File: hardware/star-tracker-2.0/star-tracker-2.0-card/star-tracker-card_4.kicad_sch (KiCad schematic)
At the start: 18 parts, among them U10 RCLAMP0504FB, U7 OSD3358-512M-BSM, Y1 ECS-240-12-30BQ-AEN-TR, Y2 ABS07-32.768KHZ-T

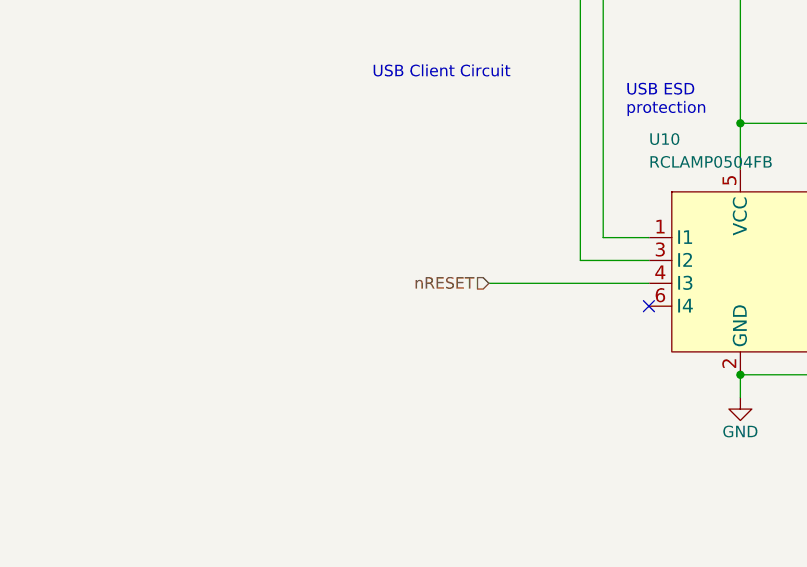
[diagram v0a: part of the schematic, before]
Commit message: Updated USB clamp
minor routing and schematic changes. Updated OPD with new transistors. Changed resistor values on LEDs.
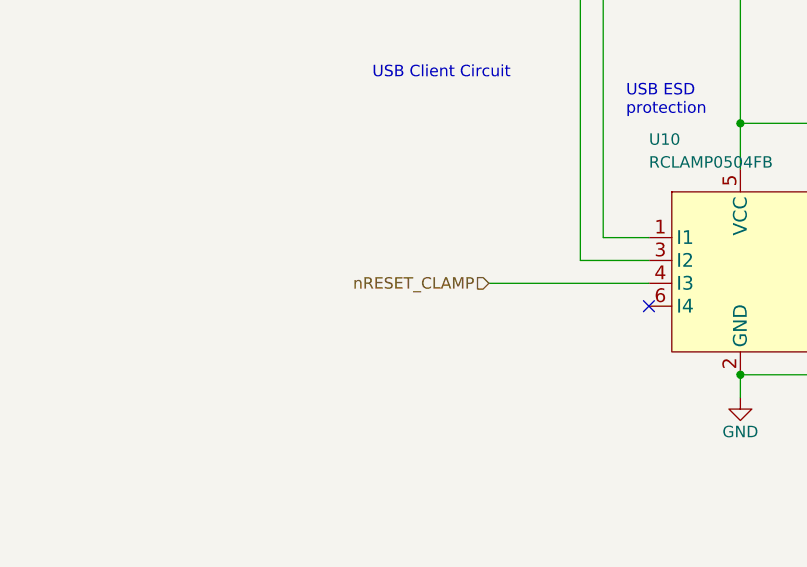
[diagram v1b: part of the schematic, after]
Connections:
- net nRESET renamed nRESET_CLAMP
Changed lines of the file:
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@@
 		)
 	)
-	(hierarchical_label "nRESET"
+	(hierarchical_label "nRESET_CLAMP"
 		(shape input)
 		(at 139.7 185.42 180)
